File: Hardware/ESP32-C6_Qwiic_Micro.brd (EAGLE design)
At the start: 25.4 x 25.4 mm, 94 parts, among them J1 USB Female Type C Connector, J4 QWIIC_RIGHT_ANGLE, Q1 20V/4.2A/52mΩ/1.4W, U1 ESP32-C6-MINI-1, U2 RT9080-33GJ5, U3 MCP73831

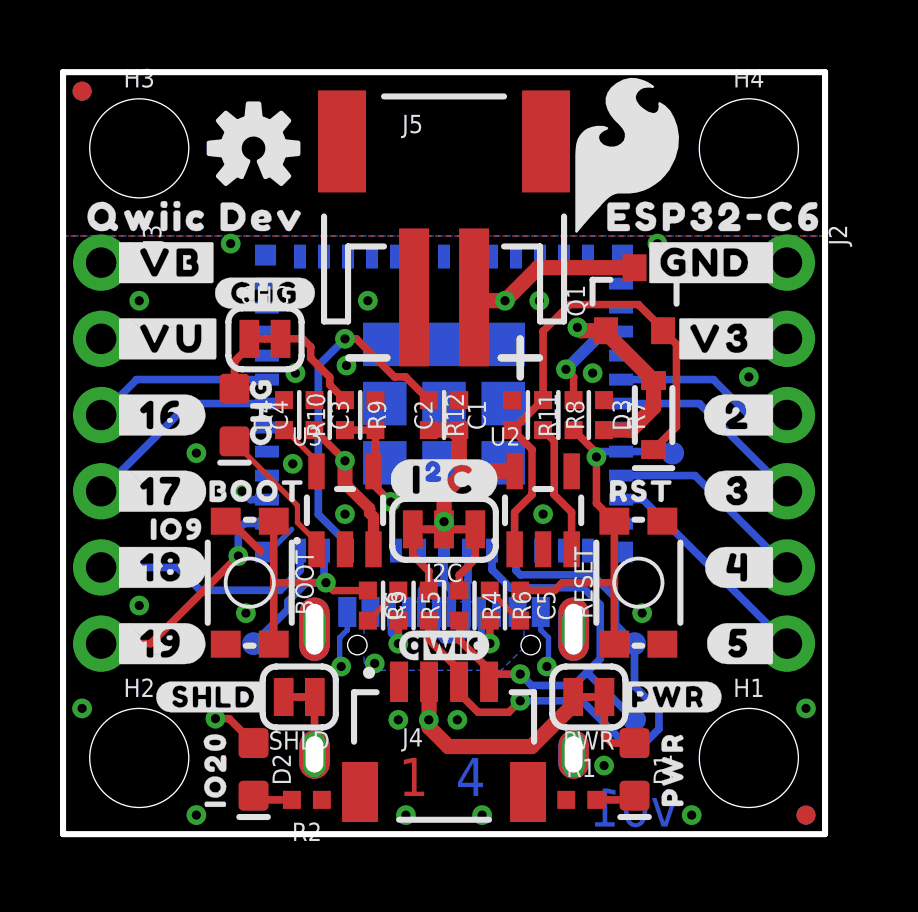
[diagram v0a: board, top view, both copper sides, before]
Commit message: Design review updates
Add voltage regulator voltage and current maximums
Add 4-layer stackup info to ordering instructions
Add info about boot button usage
Fix blue LED resistor value
Nudge N$14 to get GND to connect to battery pad
Add tRestrict between C1 and C2
Fix acid traps
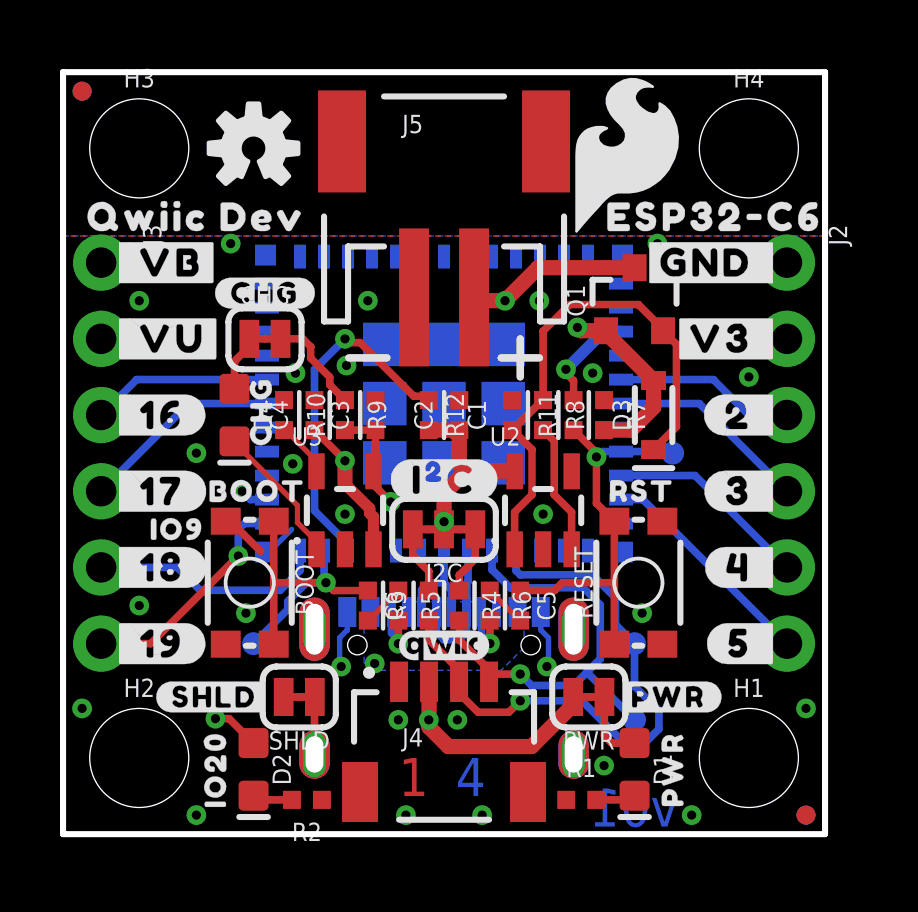
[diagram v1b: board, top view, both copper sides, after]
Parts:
- R2: value 4.7k -> 2.2k
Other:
- board text added: "4-layer JLC7628 Stackup Material: TG135-140 1oz outer layers 0.5oz inner layers Board thickness: 1.6mm Soldermask: Red Silkscreen: White Surface Finish: Lead-Free HASL"
- board text removed: "4-layer Board thickness: 1.6mm Soldermask: Red Silkscreen: White Surface Finish: Lead-Free HASL"
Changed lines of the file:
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@@
 <text x="13.589" y="1.905" size="1.27" layer="16" font="vector" ratio="15" align="center">4</text>
 <text x="38.1" y="40.64" size="1.778" layer="51" font="vector" align="top-left">4-layer
+JLC7628 Stackup
+Material: TG135-140
+1oz outer layers
+0.5oz inner layers
 Board thickness: 1.6mm
 Soldermask: Red
 Silkscreen: White
 Surface Finish: Lead-Free HASL</text>
+<rectangle x1="13.716" y1="13.843" x2="14.478" y2="14.097" layer="41"/>
 </plain>
 <attributes>
@@
 <attribute name="VALUE" x="17.272" y="0.381" size="0.6096" layer="27" font="vector" ratio="20" align="top-center"/>
 </element>
-<element name="R2" library="SparkFun-Resistors" package="0402-TIGHT" value="4.7k" x="8.128" y="1.143" smashed="yes" rot="R180">
+<element name="R2" library="SparkFun-Resistors" package="0402-TIGHT" value="2.2k" x="8.128" y="1.143" smashed="yes" rot="R180">
 <attribute name="NAME" x="8.128" y="0.381" size="0.6096" layer="25" font="vector" ratio="20" rot="R180" align="bottom-center"/>
-<attribute name="PROD_ID" value="RES-15343" x="8.128" y="1.143" size="1.778" layer="27" font="vector" ratio="15" rot="R180" display="off"/>
-<attribute name="VALUE" x="8.128" y="1.905" size="0.6096" layer="27" font="vector" ratio="20" rot="R180" align="top-center"/>
+<attribute name="PROD_ID" value="RES-14341" x="8.128" y="1.143" size="1.778" layer="27" font="vector" ratio="15" rot="R180" display="off"/>
+<attribute name="VALUE" value="2.2k" x="8.128" y="1.905" size="0.6096" layer="27" font="vector" ratio="20" rot="R180" align="top-center"/>
 </element>
 <element name="PWR" library="SparkFun-Jumpers" package="SMT-JUMPER_2_NC_TRACE_SILK" package3d_urn="urn:adsk.eagle:package:39281/1" value="JUMPER-SMT_2_NC_TRACE_SILK" x="17.526" y="4.572" smashed="yes" rot="R180">
@@
 <wire x1="12.7" y1="11.3552" x2="13.4399" y2="12.0951" width="0.508" layer="1"/>
 <via x="16.764" y="15.494" extent="1-16" drill="0.3048"/>
-<wire x1="16.764" y1="15.494" x2="17.018" y2="15.24" width="0.254" layer="1"/>
-<wire x1="17.018" y1="15.24" x2="17.018" y2="14.47" width="0.254" layer="1"/>
+<wire x1="16.764" y1="15.494" x2="16.764" y2="15.367" width="0.254" layer="1"/>
+<wire x1="17.018" y1="15.113" x2="16.764" y2="15.367" width="0.254" layer="1"/>
+<wire x1="17.018" y1="15.113" x2="17.018" y2="14.47" width="0.254" layer="1"/>
 <wire x1="18.021" y1="16.751" x2="16.764" y2="15.494" width="0.381" layer="16"/>
 <wire x1="18.021" y1="16.751" x2="18.6" y2="16.751" width="0.381" layer="16"/>
@@
 <contactref element="R12" pad="1"/>
 <wire x1="9.5" y1="9.451" x2="9.5" y2="9.66796875" width="0.254" layer="16"/>
-<wire x1="8.509" y1="10.65896875" x2="8.509" y2="15.621" width="0.254" layer="16"/>
-<wire x1="9.5" y1="9.66796875" x2="8.509" y2="10.65896875" width="0.254" layer="16"/>
-<wire x1="8.509" y1="15.621" x2="9.398" y2="16.51" width="0.254" layer="16"/>
+<wire x1="8.382" y1="10.78596875" x2="8.382" y2="15.494" width="0.254" layer="16"/>
+<wire x1="9.5" y1="9.66796875" x2="8.382" y2="10.78596875" width="0.254" layer="16"/>
+<wire x1="8.382" y1="15.494" x2="9.398" y2="16.51" width="0.254" layer="16"/>
 <via x="9.398" y="16.51" extent="1-16" drill="0.3048"/>
-<wire x1="11.049" y1="15.24" x2="9.779" y2="16.51" width="0.254" layer="1"/>
-<wire x1="9.398" y1="16.51" x2="9.779" y2="16.51" width="0.254" layer="1"/>
-<wire x1="11.422" y1="15.24" x2="12.192" y2="14.47" width="0.254" layer="1"/>
-<wire x1="11.049" y1="15.24" x2="11.422" y2="15.24" width="0.254" layer="1"/>
+<wire x1="9.398" y1="16.51" x2="9.525" y2="16.383" width="0.254" layer="1"/>
+<wire x1="9.906" y1="16.383" x2="9.525" y2="16.383" width="0.254" layer="1"/>
+<wire x1="12.065" y1="14.597" x2="12.192" y2="14.47" width="0.254" layer="1"/>
+<wire x1="12.065" y1="14.597" x2="11.692" y2="14.597" width="0.254" layer="1"/>
+<wire x1="11.692" y1="14.597" x2="9.906" y2="16.383" width="0.254" layer="1"/>
 </signal>
 <signal name="IO4">
